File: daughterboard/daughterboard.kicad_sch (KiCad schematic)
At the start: 8 parts, among them J1 Conn_01x30, J2 Conn_01x02_Female, U1 YAAJ_WeAct_BlackPill_Part_Lik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

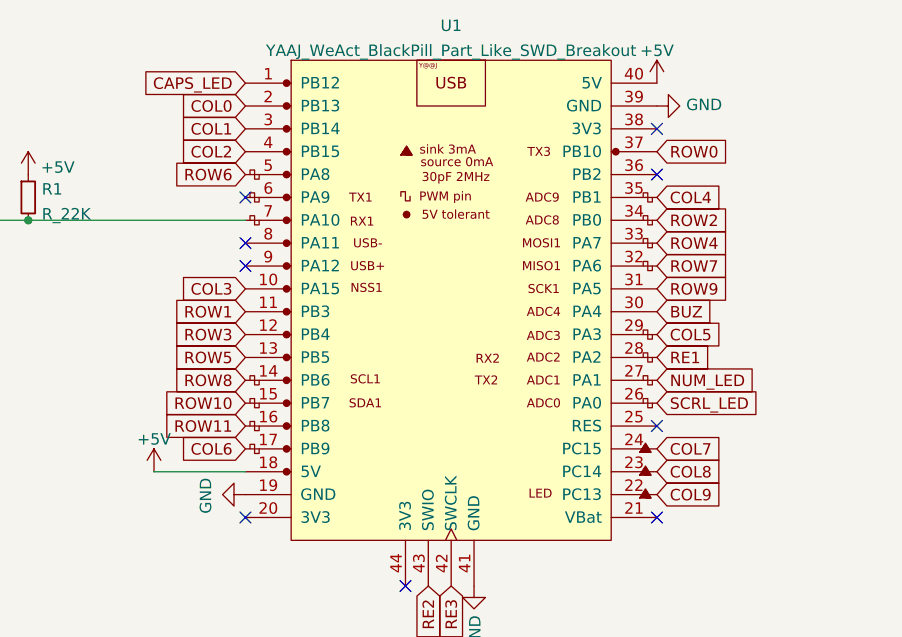
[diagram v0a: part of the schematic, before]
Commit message: daughterboard rewire
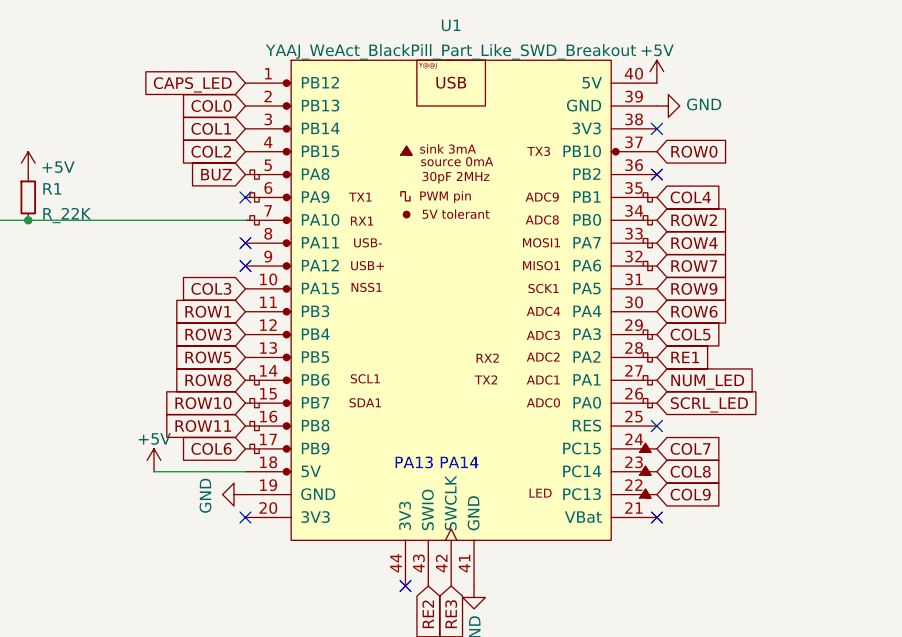
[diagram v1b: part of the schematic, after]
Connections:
- net BUZ: now also U1.5 (PA8); no longer U1.30 (PA4)
- net ROW6: now also U1.30 (PA4); no longer U1.5 (PA8)
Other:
- note added: "PA13 PA14"
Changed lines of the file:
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@@
     (stroke (width 0) (type default) (color 0 0 0 0))
   )
+  (text "PA13 PA14" (at 91.44 115.57 0)
+    (effects (font (size 1.27 1.27)) (justify left bottom))
+  )
   (global_label "RE1" (shape input) (at 120.65 102.87 0) (fields_autoplaced)
     (effects (font (size 1.27 1.27)) (justify left))
@@
     )
   )
-  (global_label "ROW6" (shape input) (at 74.93 82.55 180) (fields_autoplaced)
-    (effects (font (size 1.27 1.27)) (justify right))
-    (property "Intersheet References" "${INTERSHEET_REFS}" (id 0) (at 67.2555 82.4706 0)
-      (effects (font (size 1.27 1.27)) (justify right) hide)
+  (global_label "ROW6" (shape input) (at 120.65 97.79 0) (fields_autoplaced)
+    (effects (font (size 1.27 1.27)) (justify left))
+    (property "Intersheet References" "${INTERSHEET_REFS}" (id 0) (at 128.3245 97.8694 0)
+      (effects (font (size 1.27 1.27)) (justify left) hide)
     )
   )
@@
     )
   )
-  (global_label "BUZ" (shape input) (at 120.65 97.79 0) (fields_autoplaced)
-    (effects (font (size 1.27 1.27)) (justify left))
-    (property "Intersheet References" "${INTERSHEET_REFS}" (id 0) (at 126.7842 97.8694 0)
-      (effects (font (size 1.27 1.27)) (justify left) hide)
-    )
-  )
+  (global_label "BUZ" (shape input) (at 74.93 82.55 180) (fields_autoplaced)
+    (effects (font (size 1.27 1.27)) (justify right))
+    (property "Intersheet References" "${INTERSHEET_REFS}" (id 0) (at 68.7958 82.4706 0)
+      (effects (font (size 1.27 1.27)) (justify right) hide)
+    )
+  )

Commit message: v3 with 10u support
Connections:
- net GND: no longer U1.41 (GND)
- no-connect marks 9 -> 10
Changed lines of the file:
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@@
   (no_connect (at 120.65 82.55))
   (no_connect (at 74.93 90.17))
+  (no_connect (at 100.33 128.27))
   (no_connect (at 74.93 85.09))
   (wire (pts (xy 64.77 115.57) (xy 74.93 115.57))
@@
     )
     (property "Datasheet" "" (id 3) (at 112.395 34.925 0)
-      (effects (font (size 1.27 1.27)) hide)
-    )
-    (pin "1")
-  )
-  (symbol (lib_id "kicad_port-rescue:GND-power") (at 100.33 128.27 0) (unit 1)
-    (in_bom yes) (on_board yes)
-    (property "Reference" "#PWR0106" (id 0) (at 100.33 134.62 0)
-      (effects (font (size 1.27 1.27)) hide)
-    )
-    (property "Value" "GND" (id 1) (at 100.457 131.5212 90)
-      (effects (font (size 1.27 1.27)) (justify right))
-    )
-    (property "Footprint" "" (id 2) (at 100.33 128.27 0)
-      (effects (font (size 1.27 1.27)) hide)
-    )
-    (property "Datasheet" "" (id 3) (at 100.33 128.27 0)
       (effects (font (size 1.27 1.27)) hide)
     )
@@
       (reference "#PWR0105") (unit 1) (value "GND") (footprint "")
     )
-    (path "/a320faa1-73a3-402b-83ed-2307e7de7bab"
-      (reference "#PWR0106") (unit 1) (value "GND") (footprint "")
-    )
     (path "/3d243fdb-41fd-499a-9e6c-1ff5343cde77"

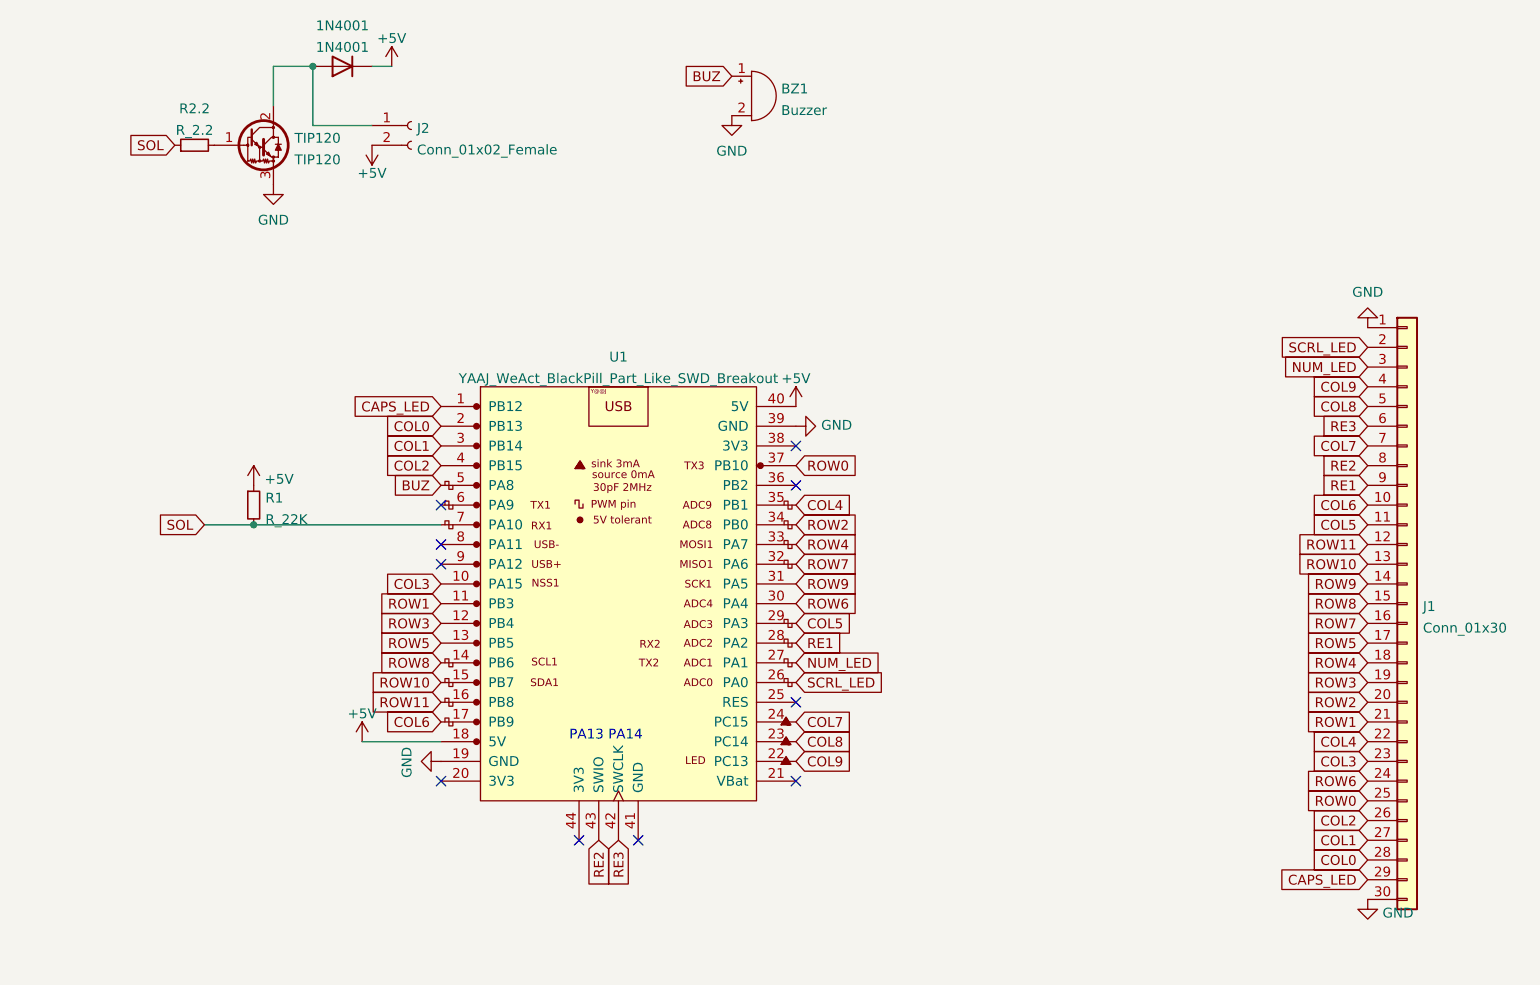
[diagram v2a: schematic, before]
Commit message: Fix ortho diode
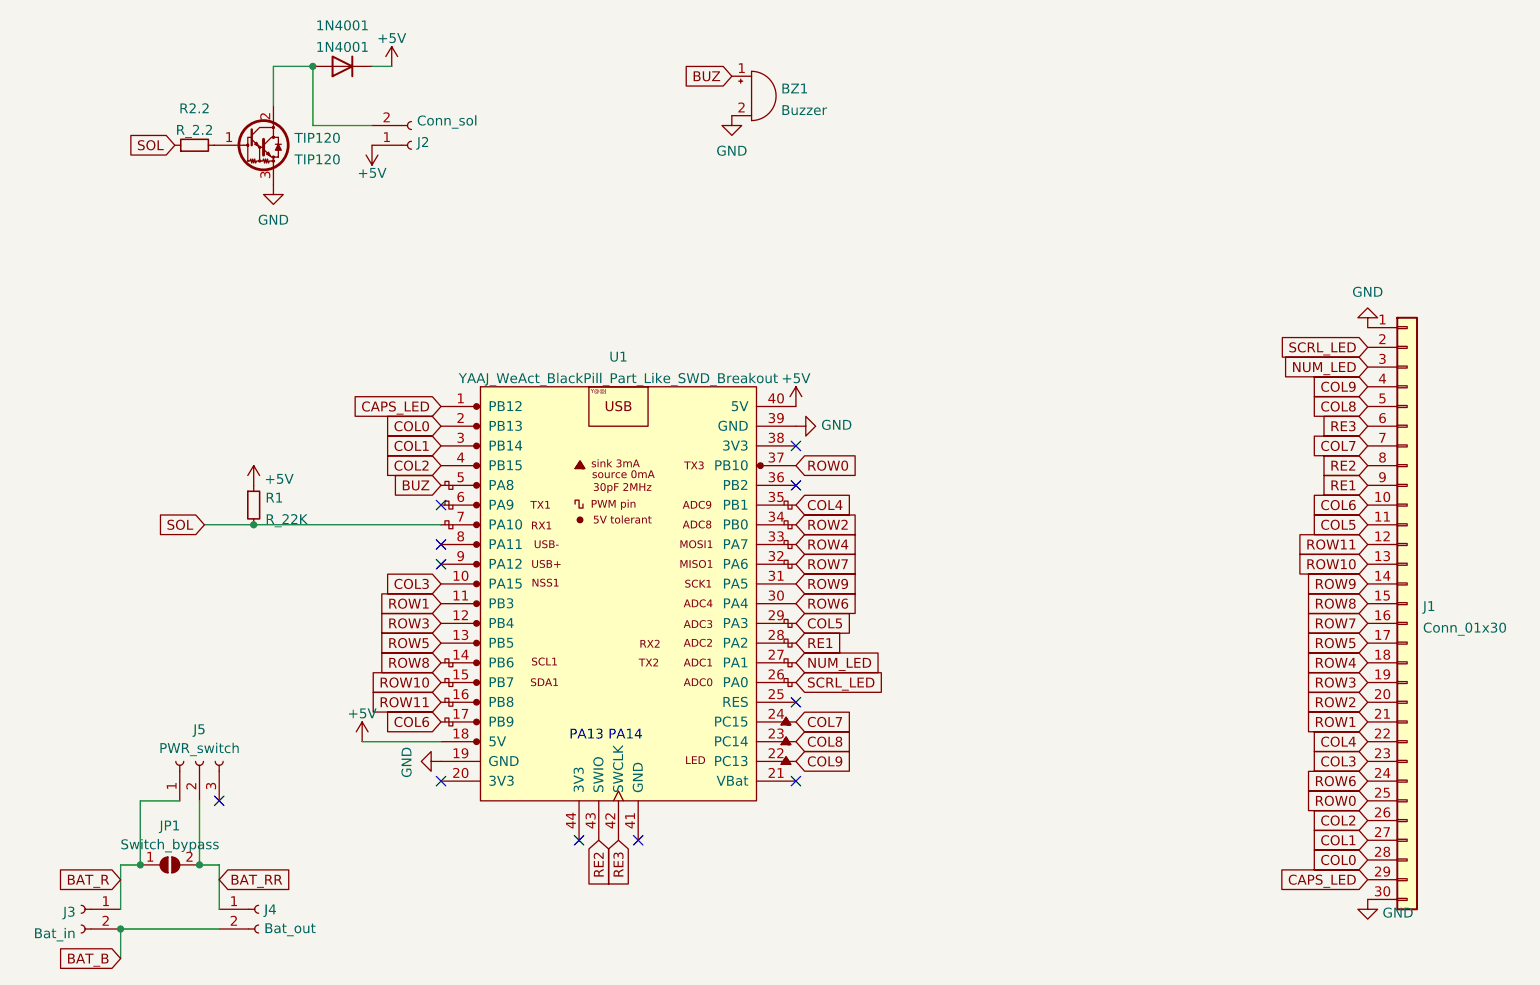
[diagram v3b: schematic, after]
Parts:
- added J3: Bat_in, Connector_PinHeader_2.54mm:PinHeader_1x02_P2.54mm_Vertical, symbol Connector:Conn_01x02_Female
- added J4: Bat_out, Connector_PinHeader_2.54mm:PinHeader_1x02_P2.54mm_Vertical, symbol Connector:Conn_01x02_Female
- added J5: PWR_switch, symbol Connector:Conn_01x03_Socket
- added JP1: Switch_bypass, symbol Jumper:SolderJumper_2_Open
- J2: value Conn_01x02_Female -> Conn_sol
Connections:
- net +5V: now also J2.1 (Pin_1); no longer J2.2 (Pin_2)
- net at 1N4001.2 (A), TIP120.2 (C): now also J2.2 (Pin_2); no longer J2.1 (Pin_1)
- new net BAT_B: J3.2 (Pin_2), J4.2 (Pin_2)
- new net BAT_R: J3.1 (Pin_1), J5.1 (Pin_1), JP1.1 (A)
- new net BAT_RR: J4.1 (Pin_1), J5.2 (Pin_2), JP1.2 (B)
- no-connect marks 10 -> 11
